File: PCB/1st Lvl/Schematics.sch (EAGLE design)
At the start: 53 parts, among them U1 TPS73533, U10 MSP430FR5969V2, U11 SPARKFUN_USD-SOCKETSMD, U12 SN74CB3T1G125_DCK_5, U13 AS3930, U2 BQ24072_RGT_16, U3 BQ27410-G1_DRZ_12, U4 LSM303DLHC, U5 BU4S66G2, U6 L3GD20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

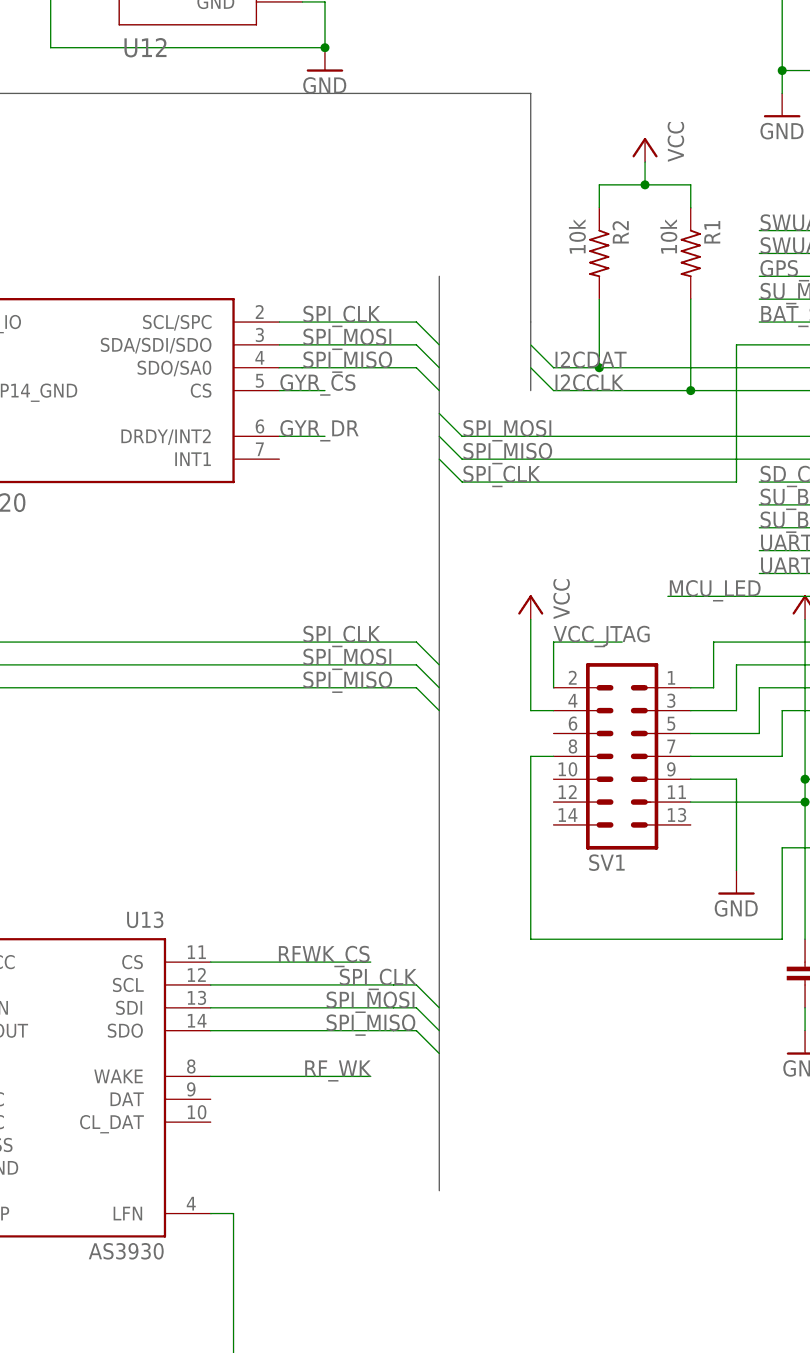
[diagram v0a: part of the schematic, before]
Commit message: Modified 1st lvl schematic, changed gyro to i2c, board still needs update
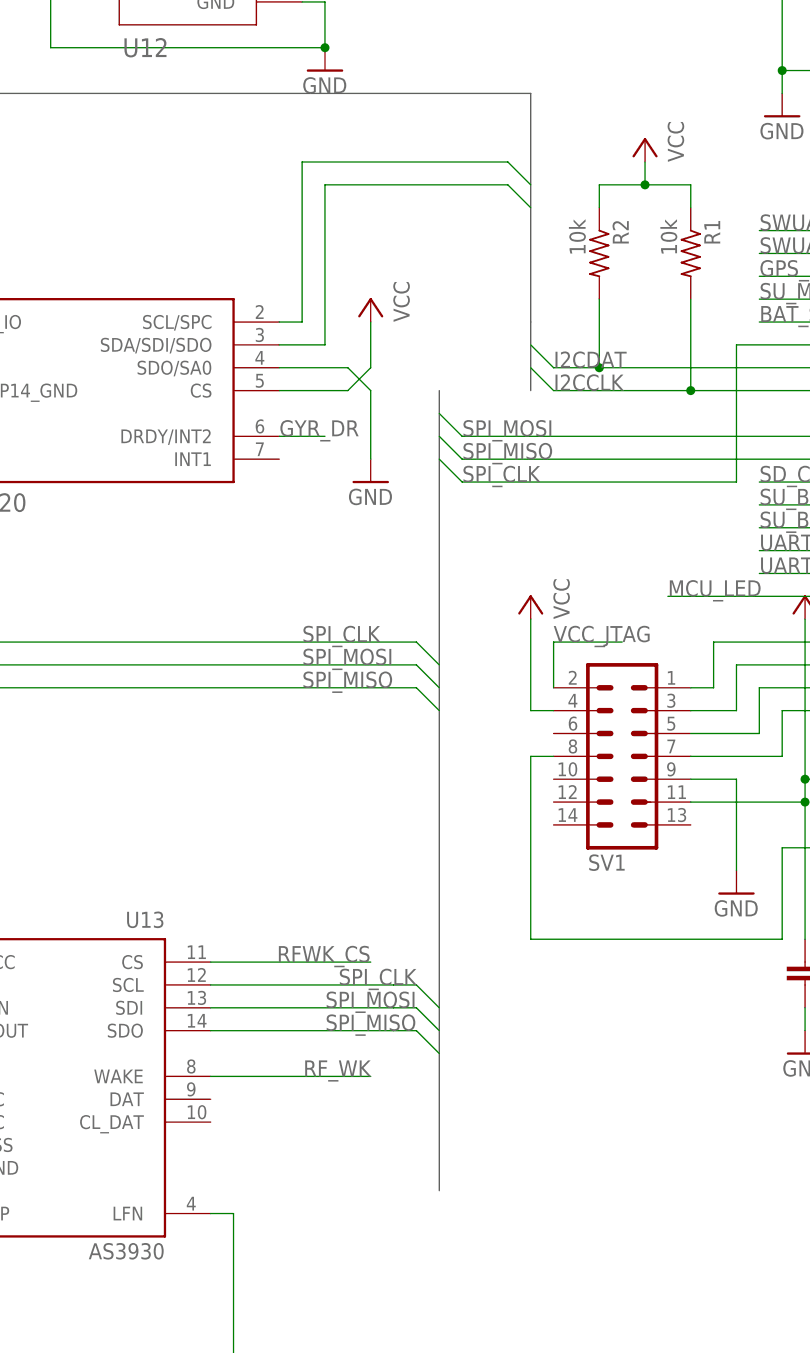
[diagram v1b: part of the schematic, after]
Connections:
- net GND: now also U6.SDO/SA0
- net GYR_CS: no longer U6.CS
- net I2CCLK: now also U6.SCL/SPC
- net I2CDAT: now also U6.SDA/SDI/SDO
- net SPI_CLK: no longer U6.SCL/SPC
- net SPI_MISO: no longer U6.SDO/SA0
- net SPI_MOSI: no longer U6.SDA/SDI/SDO
- net VCC: now also U6.CS
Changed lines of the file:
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@@
 <part name="GND12" library="supply1" deviceset="GND" device=""/>
 <part name="GND13" library="supply1" deviceset="GND" device=""/>
+<part name="VDD6" library="supply1" deviceset="VCC" device=""/>
+<part name="GND14" library="supply1" deviceset="GND" device=""/>
 </parts>
 <sheets>
@@
 <instance part="GND12" gate="1" x="-35.56" y="58.42"/>
 <instance part="GND13" gate="1" x="-35.56" y="38.1"/>
+<instance part="VDD6" gate="VCC" x="-30.48" y="12.7" rot="MR0"/>
+<instance part="GND14" gate="1" x="-30.48" y="-7.62"/>
 </instances>
 <busses>
@@
 <bus name="SPI_CLK,SPI_MOSI,SPI_MISO">
 <segment>
-<wire x1="-22.86" y1="15.24" x2="-22.86" y2="-86.36" width="0.762" layer="92"/>
+<wire x1="-22.86" y1="2.54" x2="-22.86" y2="-86.36" width="0.762" layer="92"/>
 </segment>
 </bus>
@@
 <junction x="-35.56" y="40.64"/>
 </segment>
+<segment>
+<pinref part="U6" gate="G$1" pin="SDO/SA0"/>
+<wire x1="-40.64" y1="5.08" x2="-33.02" y2="5.08" width="0.1524" layer="91"/>
+<wire x1="-33.02" y1="5.08" x2="-30.48" y2="2.54" width="0.1524" layer="91"/>
+<pinref part="GND14" gate="1" pin="GND"/>
+<wire x1="-30.48" y1="2.54" x2="-30.48" y2="-5.08" width="0.1524" layer="91"/>
+</segment>
 </net>
 <net name="AGND" class="0">
@@
 <wire x1="5.08" y1="25.4" x2="5.08" y2="22.86" width="0.1524" layer="91"/>
 </segment>
+<segment>
+<pinref part="U6" gate="G$1" pin="CS"/>
+<wire x1="-40.64" y1="2.54" x2="-33.02" y2="2.54" width="0.1524" layer="91"/>
+<wire x1="-33.02" y1="2.54" x2="-30.48" y2="5.08" width="0.1524" layer="91"/>
+<pinref part="VDD6" gate="VCC" pin="VCC"/>
+<wire x1="-30.48" y1="5.08" x2="-30.48" y2="10.16" width="0.1524" layer="91"/>
+</segment>
 </net>
 <net name="I2CCLK" class="0">
@@
 <wire x1="-76.2" y1="68.58" x2="-63.5" y2="68.58" width="0.1524" layer="91"/>
 </segment>
+<segment>
+<pinref part="U6" gate="G$1" pin="SCL/SPC"/>
+<wire x1="-40.64" y1="10.16" x2="-38.1" y2="10.16" width="0.1524" layer="91"/>
+<wire x1="-38.1" y1="10.16" x2="-38.1" y2="27.94" width="0.1524" layer="91"/>
+<wire x1="-38.1" y1="27.94" x2="-15.24" y2="27.94" width="0.1524" layer="91"/>
+<wire x1="-12.7" y1="25.4" x2="-15.24" y2="27.94" width="0.1524" layer="91"/>
+</segment>
 </net>
 <net name="I2CDAT" class="0">
@@
 <wire x1="-76.2" y1="48.26" x2="-63.5" y2="48.26" width="0.1524" layer="91"/>
 </segment>
+<segment>
+<pinref part="U6" gate="G$1" pin="SDA/SDI/SDO"/>
+<wire x1="-40.64" y1="7.62" x2="-35.56" y2="7.62" width="0.1524" layer="91"/>
+<wire x1="-35.56" y1="7.62" x2="-35.56" y2="25.4" width="0.1524" layer="91"/>
+<wire x1="-35.56" y1="25.4" x2="-15.24" y2="25.4" width="0.1524" layer="91"/>
+<wire x1="-12.7" y1="22.86" x2="-15.24" y2="25.4" width="0.1524" layer="91"/>
+</segment>
 </net>
 <net name="N$18" class="0">
@@
 </segment>
 <segment>
-<wire x1="-25.4" y1="7.62" x2="-40.64" y2="7.62" width="0.1524" layer="91"/>
-<label x="-38.1" y="7.62" size="1.778" layer="95"/>
-<pinref part="U6" gate="G$1" pin="SDA/SDI/SDO"/>
-<wire x1="-25.4" y1="7.62" x2="-22.86" y2="5.08" width="0.1524" layer="91"/>
-</segment>
-<segment>
 <wire x1="-48.26" y1="-66.04" x2="-27.94" y2="-66.04" width="0.1524" layer="91"/>
 <label x="-25.4" y="-66.04" size="1.778" layer="95" rot="MR0"/>
@@
 <wire x1="-20.32" y1="-5.08" x2="-22.86" y2="-2.54" width="0.1524" layer="91"/>
 <pinref part="U10" gate="G$1" pin="25_P2.1"/>
-</segment>
-<segment>
-<wire x1="-25.4" y1="5.08" x2="-38.1" y2="5.08" width="0.1524" layer="91"/>
-<wire x1="-38.1" y1="5.08" x2="-40.64" y2="5.08" width="0.1524" layer="91"/>
-<label x="-38.1" y="5.08" size="1.778" layer="95"/>
-<pinref part="U6" gate="G$1" pin="SDO/SA0"/>
-<wire x1="-25.4" y1="5.08" x2="-22.86" y2="2.54" width="0.1524" layer="91"/>
 </segment>
 <segment>
@@
 </segment>
 <segment>
-<wire x1="-25.4" y1="10.16" x2="-40.64" y2="10.16" width="0.1524" layer="91"/>
-<label x="-38.1" y="10.16" size="1.778" layer="95"/>
-<pinref part="U6" gate="G$1" pin="SCL/SPC"/>
-<wire x1="-25.4" y1="10.16" x2="-22.86" y2="7.62" width="0.1524" layer="91"/>
-</segment>
-<segment>
 <wire x1="-48.26" y1="-63.5" x2="-27.94" y2="-63.5" width="0.1524" layer="91"/>
 <label x="-25.4" y="-63.5" size="1.778" layer="95" rot="MR0"/>
@@
 <pinref part="U10" gate="G$1" pin="4_P3.0"/>
 </segment>
-<segment>
-<pinref part="U6" gate="G$1" pin="CS"/>
-<wire x1="-40.64" y1="2.54" x2="-35.56" y2="2.54" width="0.1524" layer="91"/>
-<label x="-40.64" y="2.54" size="1.778" layer="95"/>
-</segment>
-</net>
+</net>
